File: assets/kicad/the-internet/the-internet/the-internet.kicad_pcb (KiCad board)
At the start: 2 copper layers, 66 x 50.8 mm, 34 parts, among them J1 LED connector, J2 Battery, Q1 IRF9240, Q2 BC547, Q3 BC547, Q4 BC547, Q6 BC557, Q7 BC557, Q8 BC547, SW1 NO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

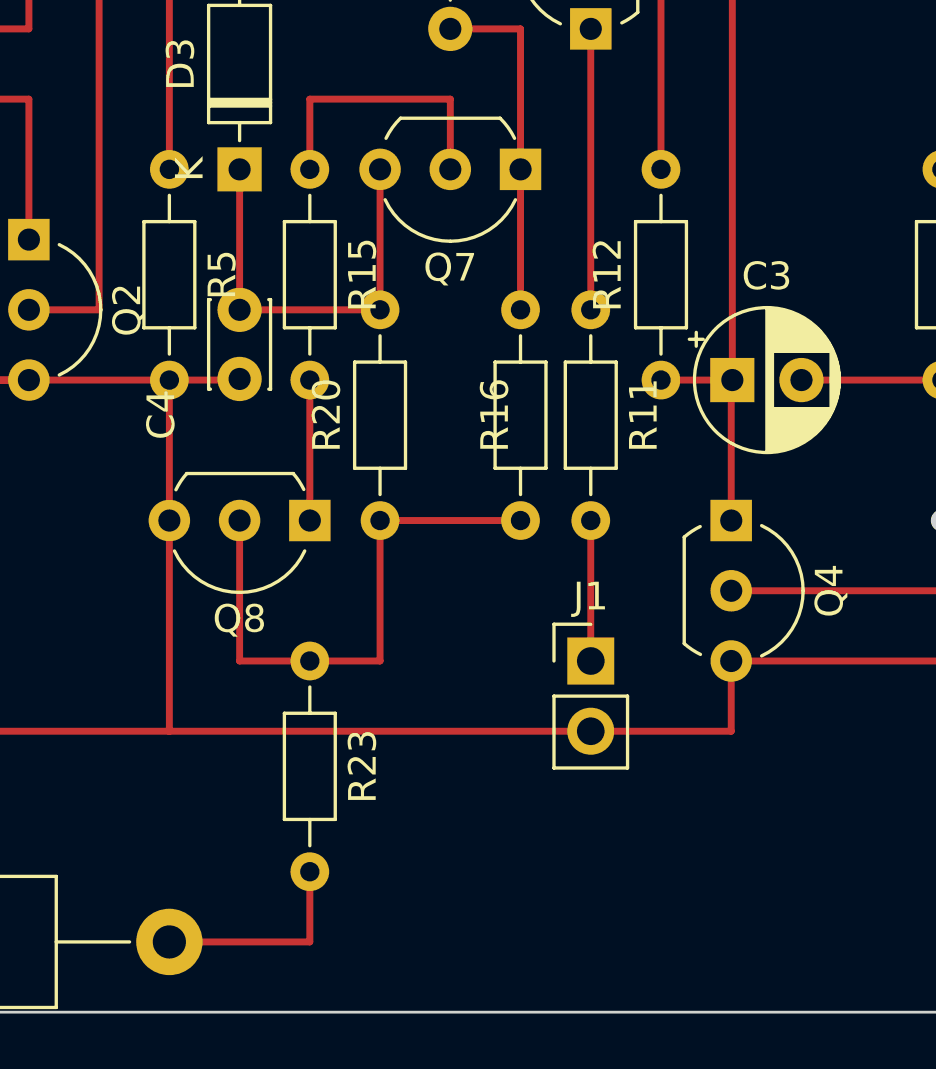
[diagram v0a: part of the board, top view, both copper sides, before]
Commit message: Added signal terminal
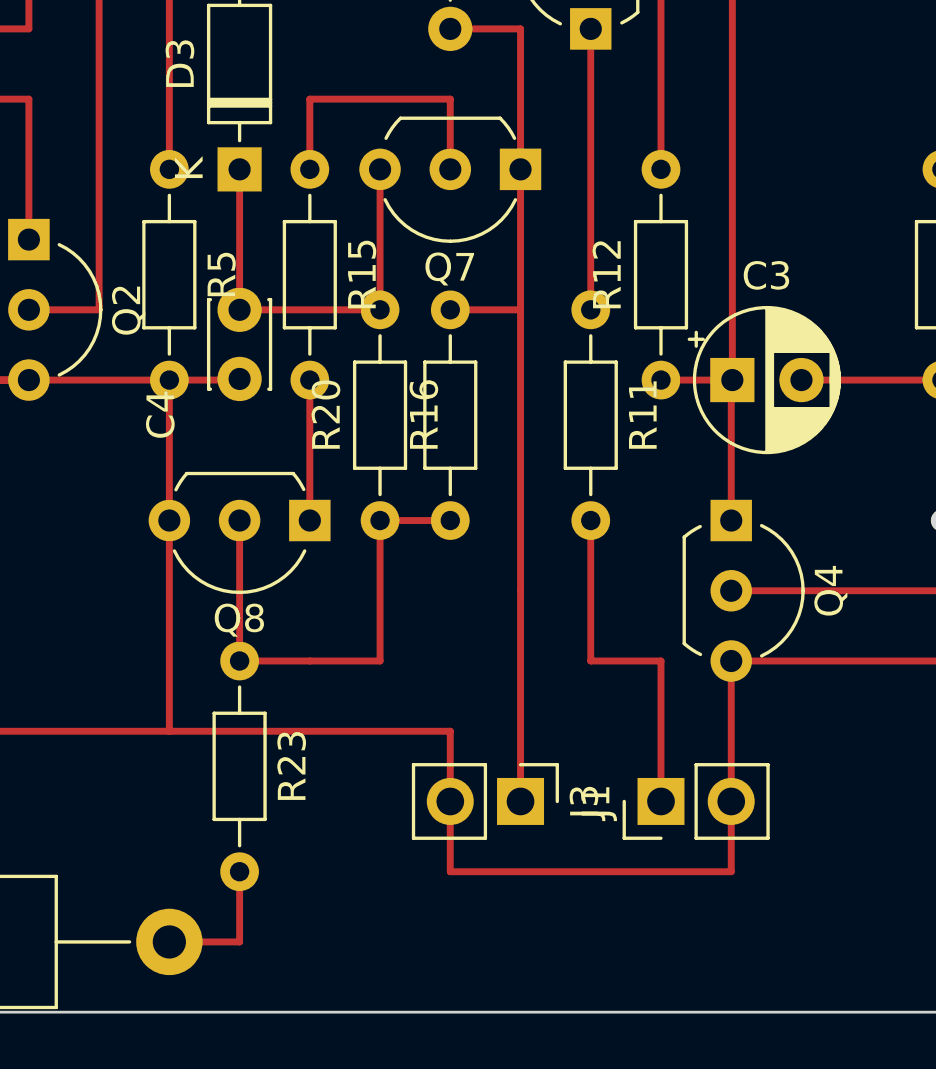
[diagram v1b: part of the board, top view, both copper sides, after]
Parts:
- added J3: Signal, Connector_PinHeader_2.54mm:PinHeader_1x02_P2.54mm_Vertical, F.Cu at (86.4, 124.5)
- moved J1 5.68 mm to (91.4, 124.5), turned to 90 degrees
- moved R16 2.54 mm to (83.8, 114.3)
- moved R23 2.54 mm to (76.2, 119.4)
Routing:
- net signal: track 12.7 -> 33.0 mm
- net GND: track 132.1 -> 142.3 mm
- net Net-(J1-Pin_1): track 5.08 -> 12.7 mm
- net Net-(Q8-B): track 20.3 -> 17.8 mm
- net Net-(R23-Pad2): track 7.62 -> 5.08 mm

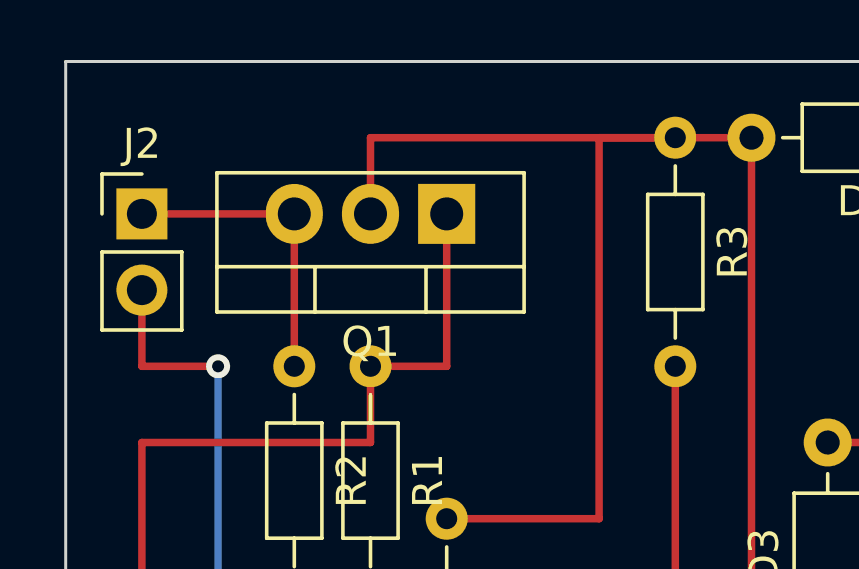
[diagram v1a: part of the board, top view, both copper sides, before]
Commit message: Changed layout for connectors
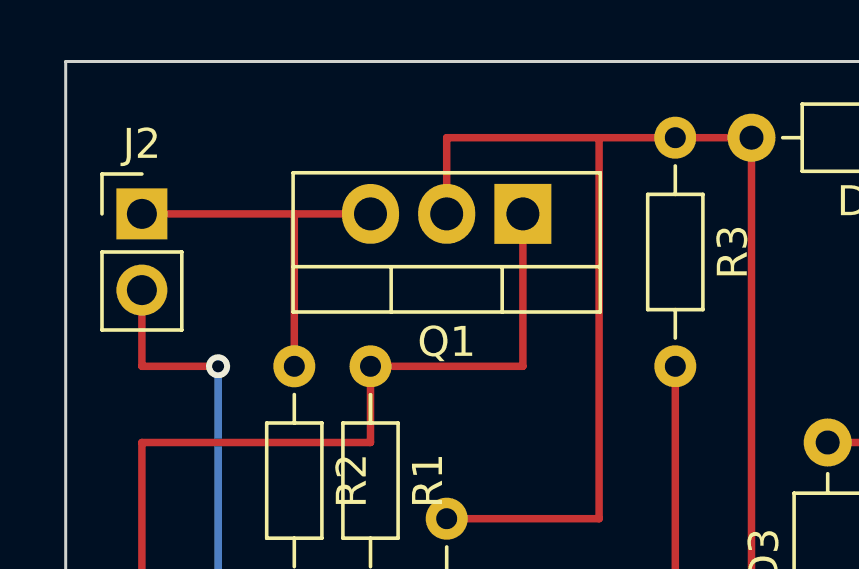
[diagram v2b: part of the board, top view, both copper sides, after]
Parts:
- moved Q1 2.54 mm to (66.0, 86.4)
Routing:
- net Net-(D4-A): track 53.3 -> 48.3 mm
- net Net-(Q1-G): track 31.1 -> 33.6 mm
- net Vbat: track 10.2 -> 12.7 mm
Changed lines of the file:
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@@
   )
   (footprint "Package_TO_SOT_THT:TO-220-3_Vertical" placed (layer "F.Cu")
-    (at 63.5 86.36 180)
+    (at 66.04 86.36 180)
     (descr "TO-220-3, Vertical, RM 2.54mm, see https://www.vishay.com/docs/66542/to-220-1.pdf")
     (tags "TO-220-3 Vertical RM 2.54mm")
@@
   (segment (start 104.14 86.36) (end 104.14 93.98) (width 0.25) (layer "F.Cu") (net 10))
   (segment (start 73.66 83.82) (end 71.12 83.82) (width 0.25) (layer "F.Cu") (net 11))
-  (segment (start 60.96 83.82) (end 71.12 83.82) (width 0.25) (layer "F.Cu") (net 11))
+  (segment (start 63.5 83.82) (end 68.58 83.82) (width 0.25) (layer "F.Cu") (net 11))
   (segment (start 68.58 96.52) (end 68.58 83.82) (width 0.25) (layer "F.Cu") (net 11))
-  (segment (start 60.96 86.36) (end 60.96 83.82) (width 0.25) (layer "F.Cu") (net 11))
   (segment (start 73.66 101.6) (end 73.66 83.82) (width 0.25) (layer "F.Cu") (net 11))
+  (segment (start 63.5 86.36) (end 63.5 83.82) (width 0.25) (layer "F.Cu") (net 11))
   (segment (start 63.5 96.52) (end 68.58 96.52) (width 0.25) (layer "F.Cu") (net 11))
   (segment (start 68.58 83.82) (end 71.12 83.82) (width 0.25) (layer "F.Cu") (net 11))
@@
   (segment (start 88.9 114.3) (end 88.9 119.38) (width 0.25) (layer "F.Cu") (net 12))
   (segment (start 60.96 93.98) (end 53.34 93.98) (width 0.25) (layer "F.Cu") (net 13))
+  (segment (start 66.04 86.36) (end 66.04 91.44) (width 0.25) (layer "F.Cu") (net 13))
+  (segment (start 66.04 91.44) (end 60.96 91.44) (width 0.25) (layer "F.Cu") (net 13))
   (segment (start 60.96 91.44) (end 60.96 93.98) (width 0.25) (layer "F.Cu") (net 13))
-  (segment (start 60.96 91.44) (end 63.5 91.44) (width 0.25) (layer "F.Cu") (net 13))
-  (segment (start 63.5 91.44) (end 63.5 86.36) (width 0.25) (layer "F.Cu") (net 13))
   (segment (start 53.34 107.26) (end 53.34 93.98) (width 0.25) (layer "F.Cu") (net 13))
-  (segment (start 58.42 86.36) (end 58.42 91.44) (width 0.25) (layer "F.Cu") (net 14))
-  (segment (start 53.34 86.36) (end 58.42 86.36) (width 0.25) (layer "F.Cu") (net 14))
+  (segment (start 60.96 86.36) (end 53.34 86.36) (width 0.25) (layer "F.Cu") (net 14))
+  (segment (start 58.42 91.44) (end 58.42 86.36) (width 0.25) (layer "F.Cu") (net 14))
   (segment (start 63.5 99.06) (end 68.58 99.06) (width 0.25) (layer "F.Cu") (net 15))
   (segment (start 58.42 99.06) (end 63.5 99.06) (width 0.25) (layer "F.Cu") (net 15))

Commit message: Added final version of the internet
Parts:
- R7: value 33k -> 68k
- R8: value 68k -> 33k
- moved C2 2.54 mm to (111.7, 109.2)
- moved Q3 2.54 mm to (111.8, 114.3)
- moved R6 2.54 mm to (111.8, 101.6)
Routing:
- net GND: track 142.3 -> 139.8 mm
- net Net-(Q4-B): track 25.4 -> 22.9 mm
- net Vcc: track 66.0 -> 63.5 mm
- net Net-(Q3-B): track 25.4 -> 22.9 mm
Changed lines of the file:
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@@
         (effects (font (size 1 1) (thickness 0.15)))
     )
-    (fp_text value "68k" (at 3.81 1.92 90) (layer "F.Fab")
+    (fp_text value "33k" (at 3.81 1.92 90) (layer "F.Fab")
         (effects (font (size 1 1) (thickness 0.15)))
     )
@@
   )
   (footprint "Capacitor_THT:CP_Radial_D5.0mm_P2.50mm" placed (layer "F.Cu")
-    (at 114.26 109.22 180)
+    (at 111.72 109.22 180)
     (descr "CP, Radial series, Radial, pin pitch=2.50mm, , diameter=5mm, Electrolytic Capacitor")
     (tags "CP Radial series Radial pin pitch 2.50mm  diameter 5mm Electrolytic Capacitor")
@@
   )
   (footprint "Package_TO_SOT_THT:TO-92L_Inline_Wide" placed (layer "F.Cu")
-    (at 114.3 114.3 -90)
+    (at 111.76 114.3 -90)
     (descr "TO-92L leads in-line (large body variant of TO-92), also known as TO-226, wide, drill 0.75mm (see https://www.diodes.com/assets/Package-Files/TO92L.pdf and http://www.ti.com/lit/an/snoa059/snoa059.pdf)")
     (tags "TO-92L Inline Wide transistor")
@@
   )
   (footprint "Resistor_THT:R_Axial_DIN0204_L3.6mm_D1.6mm_P7.62mm_Horizontal" placed (layer "F.Cu")
-    (at 114.3 101.6 90)
+    (at 111.76 101.6 90)
     (descr "Resistor, Axial_DIN0204 series, Axial, Horizontal, pin pitch=7.62mm, 0.167W, length*diameter=3.6*1.6mm^2, http://cdn-reichelt.de/documents/datenblatt/B400/1_4W%23YAG.pdf")
     (tags "Resistor Axial_DIN0204 series Axial Horizontal pin pitch 7.62mm 0.167W length 3.6mm diameter 1.6mm")
@@
         (effects (font (size 1 1) (thickness 0.15)))
     )
-    (fp_text value "33k" (at 3.81 1.92 90) (layer "F.Fab")
+    (fp_text value "68k" (at 3.81 1.92 90) (layer "F.Fab")
         (effects (font (size 1 1) (thickness 0.15)))
     )
@@
   (segment (start 93.98 127) (end 93.98 124.46) (width 0.25) (layer "F.Cu") (net 2))
   (segment (start 73.66 114.3) (end 73.66 121.92) (width 0.25) (layer "F.Cu") (net 2))
-  (segment (start 93.98 119.38) (end 114.3 119.38) (width 0.25) (layer "F.Cu") (net 2))
+  (segment (start 111.76 119.38) (end 93.98 119.38) (width 0.25) (layer "F.Cu") (net 2))
   (segment (start 73.66 121.92) (end 53.34 121.92) (width 0.25) (layer "F.Cu") (net 2))
   (segment (start 66.04 109.22) (end 68.58 109.22) (width 0.25) (layer "F.Cu") (net 2))
@@
   (via (at 55.88 99.06) (size 0.8) (drill 0.4) (layers "F.Cu" "B.Cu") (net 2))
   (segment (start 55.88 91.44) (end 55.88 99.06) (width 0.25) (layer "B.Cu") (net 2))
-  (segment (start 114.3 101.6) (end 114.3 109.18) (width 0.25) (layer "F.Cu") (net 3))
-  (segment (start 114.3 109.18) (end 114.26 109.22) (width 0.25) (layer "F.Cu") (net 3))
-  (segment (start 114.26 114.26) (end 114.3 114.3) (width 0.25) (layer "F.Cu") (net 3))
-  (segment (start 114.26 109.22) (end 114.26 114.26) (width 0.25) (layer "F.Cu") (net 3))
-  (segment (start 106.68 109.22) (end 111.76 109.22) (width 0.25) (layer "F.Cu") (net 4))
+  (segment (start 111.76 114.3) (end 111.76 109.26) (width 0.25) (layer "F.Cu") (net 3))
+  (segment (start 111.72 109.22) (end 111.72 101.64) (width 0.25) (layer "F.Cu") (net 3))
+  (segment (start 111.72 101.64) (end 111.76 101.6) (width 0.25) (layer "F.Cu") (net 3))
+  (segment (start 111.76 109.26) (end 111.72 109.22) (width 0.25) (layer "F.Cu") (net 3))
   (segment (start 93.98 116.84) (end 106.68 116.84) (width 0.25) (layer "F.Cu") (net 4))
+  (segment (start 106.68 109.22) (end 109.22 109.22) (width 0.25) (layer "F.Cu") (net 4))
   (segment (start 106.68 116.84) (end 106.68 109.22) (width 0.25) (layer "F.Cu") (net 4))
   (segment (start 94.02 91.48) (end 93.98 91.44) (width 0.25) (layer "F.Cu") (net 5))
@@
   (segment (start 109.22 114.3) (end 109.22 116.84) (width 0.25) (layer "F.Cu") (net 6))
   (segment (start 101.6 109.22) (end 96.52 109.22) (width 0.25) (layer "F.Cu") (net 6))
-  (segment (start 109.22 116.84) (end 114.3 116.84) (width 0.25) (layer "F.Cu") (net 6))
+  (segment (start 111.76 116.84) (end 109.22 116.84) (width 0.25) (layer "F.Cu") (net 6))
   (segment (start 101.6 109.22) (end 101.6 114.3) (width 0.25) (layer "F.Cu") (net 6))
   (via (at 101.6 114.3) (size 0.8) (drill 0.4) (layers "F.Cu" "B.Cu") (net 6))
@@
   (segment (start 93.98 83.82) (end 81.28 83.82) (width 0.25) (layer "F.Cu") (net 10))
   (segment (start 76.2 93.98) (end 78.74 93.98) (width 0.25) (layer "F.Cu") (net 10))
-  (segment (start 104.14 93.98) (end 114.3 93.98) (width 0.25) (layer "F.Cu") (net 10))
   (segment (start 81.28 91.44) (end 81.28 83.82) (width 0.25) (layer "F.Cu") (net 10))
   (segment (start 81.28 93.98) (end 78.74 93.98) (width 0.25) (layer "F.Cu") (net 10))
   (segment (start 88.9 91.44) (end 81.28 91.44) (width 0.25) (layer "F.Cu") (net 10))
   (segment (start 104.14 83.82) (end 104.14 86.36) (width 0.25) (layer "F.Cu") (net 10))
+  (segment (start 111.76 93.98) (end 104.14 93.98) (width 0.25) (layer "F.Cu") (net 10))
   (segment (start 93.98 83.82) (end 104.14 83.82) (width 0.25) (layer "F.Cu") (net 10))
   (segment (start 81.28 93.98) (end 81.28 91.44) (width 0.25) (layer "F.Cu") (net 10))
